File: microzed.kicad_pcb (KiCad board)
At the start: 10 copper layers, 50 x 100 mm, 334 parts, among them IC1 XC7Z020-1CLG484C, IC2 RTL8211E-VL-CG, J1 640456-3, J2 10104111-0001LF, J3 L829-1J1T-43, J4 Micro_SD_Card_Det_Hirose_DM3AT, J5 10104111-0001LF, J6 BSH-090-01-X-D-A, J7 BSH-090-01-X-D-A, Q1 MMBT3904, Q2 MMBT3904, SW1 SW_Push, U1 TLV62130RGTR, U10 MT41K256M16TW, U11 MT25QL128ABA8E12-1SIT, U12 USB3320C-EZK, U13 ASDMB-24.000MHZ-LC-T, U14 ASDMB-25.000MHZ-LC-T, U15 TXS02612RTWR, U16 CP2104-F03-GM, U2 TLV62130RGTR, U3 TLV62130RGTR, U4 TLV62130RGTR, U5 TLV62130RGTR, U6 ASDMB-33.333MHZ-LC-T, U7 TPS51206DSQR, U8 REF3012, U9 MT41K256M16TW

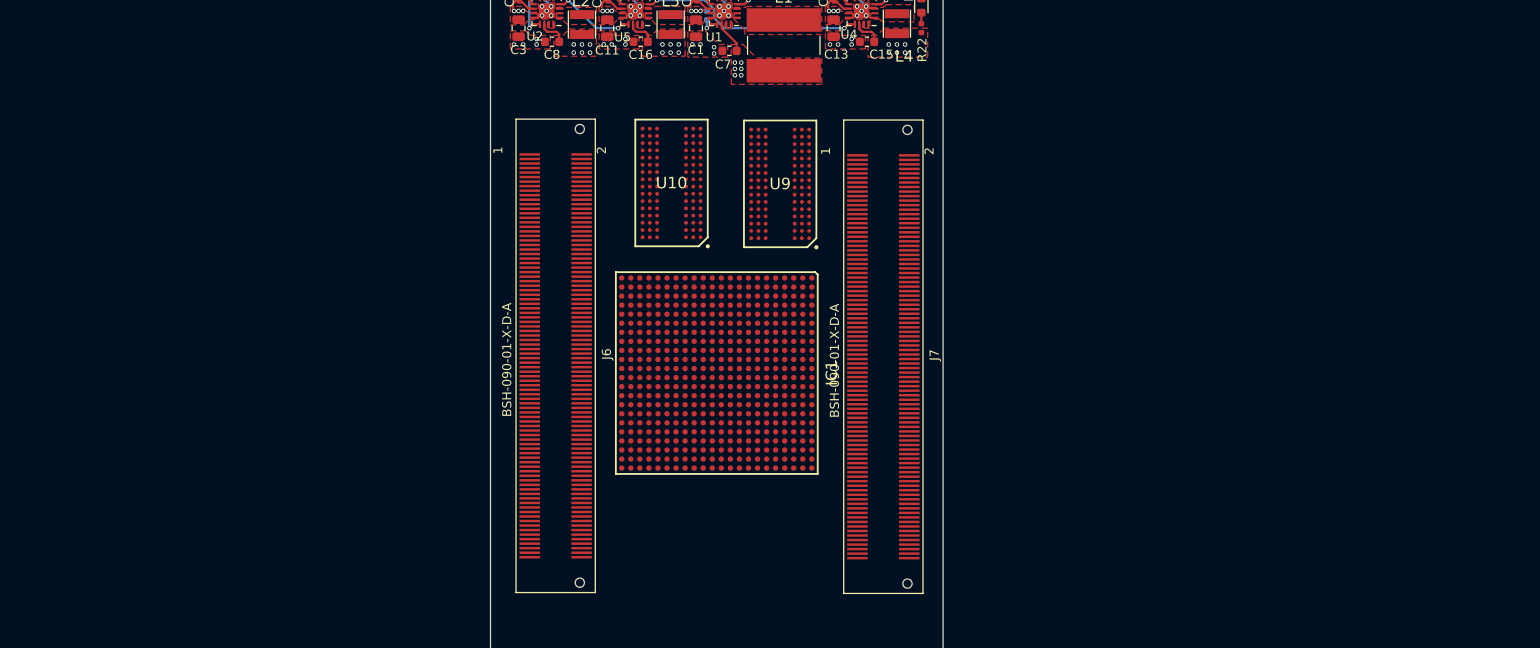
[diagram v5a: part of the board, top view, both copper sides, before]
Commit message: fix footprint & 3d model for xc7z020-clg484. (pin pitch 1.0mm -> 0.8mm)
Signed-off-by: Yi Qingliang <niqingliang2003@gmail.com>
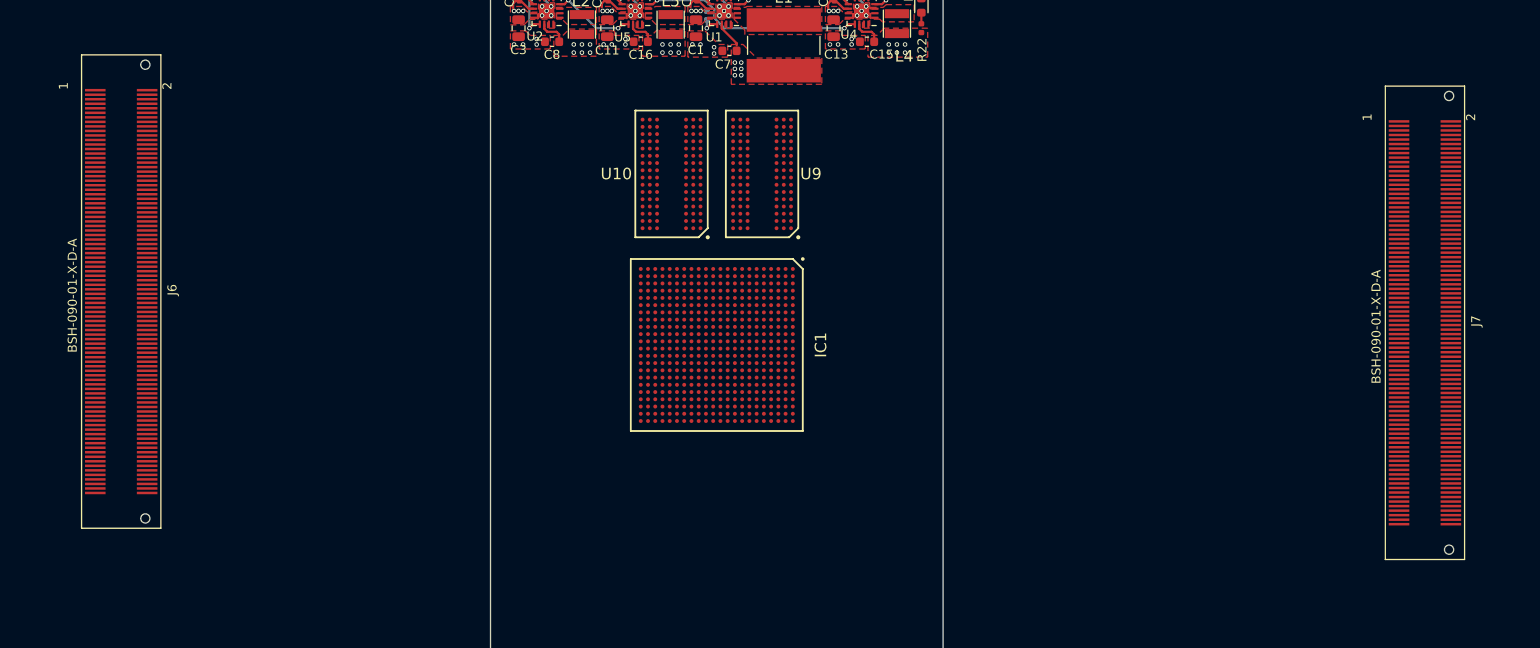
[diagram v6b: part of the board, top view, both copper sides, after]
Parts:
- IC1: footprint microzed:BGA484C100P22X22_2300X2300X254 -> microzed:BGA-484_19.0x19.0mm_Layout22x22_P0.8mm
- moved J7 60.0 mm to (78.2, 44.5)
- moved J6 48.5 mm to (-65.8, 41.0)
- moved IC1 3.10 mm to (0.00, 46.9)
- moved U9 2.28 mm to (5.00, 28.0)
- moved U10 1.00 mm to (-5.00, 28.0)

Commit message: misc update
Signed-off-by: Yi Qingliang <niqingliang2003@gmail.com>
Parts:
- J6, J7: moved to B.Cu
- moved J7 59.8 mm to (18.4, 43.7)
- moved J6 47.5 mm to (-18.4, 43.7)

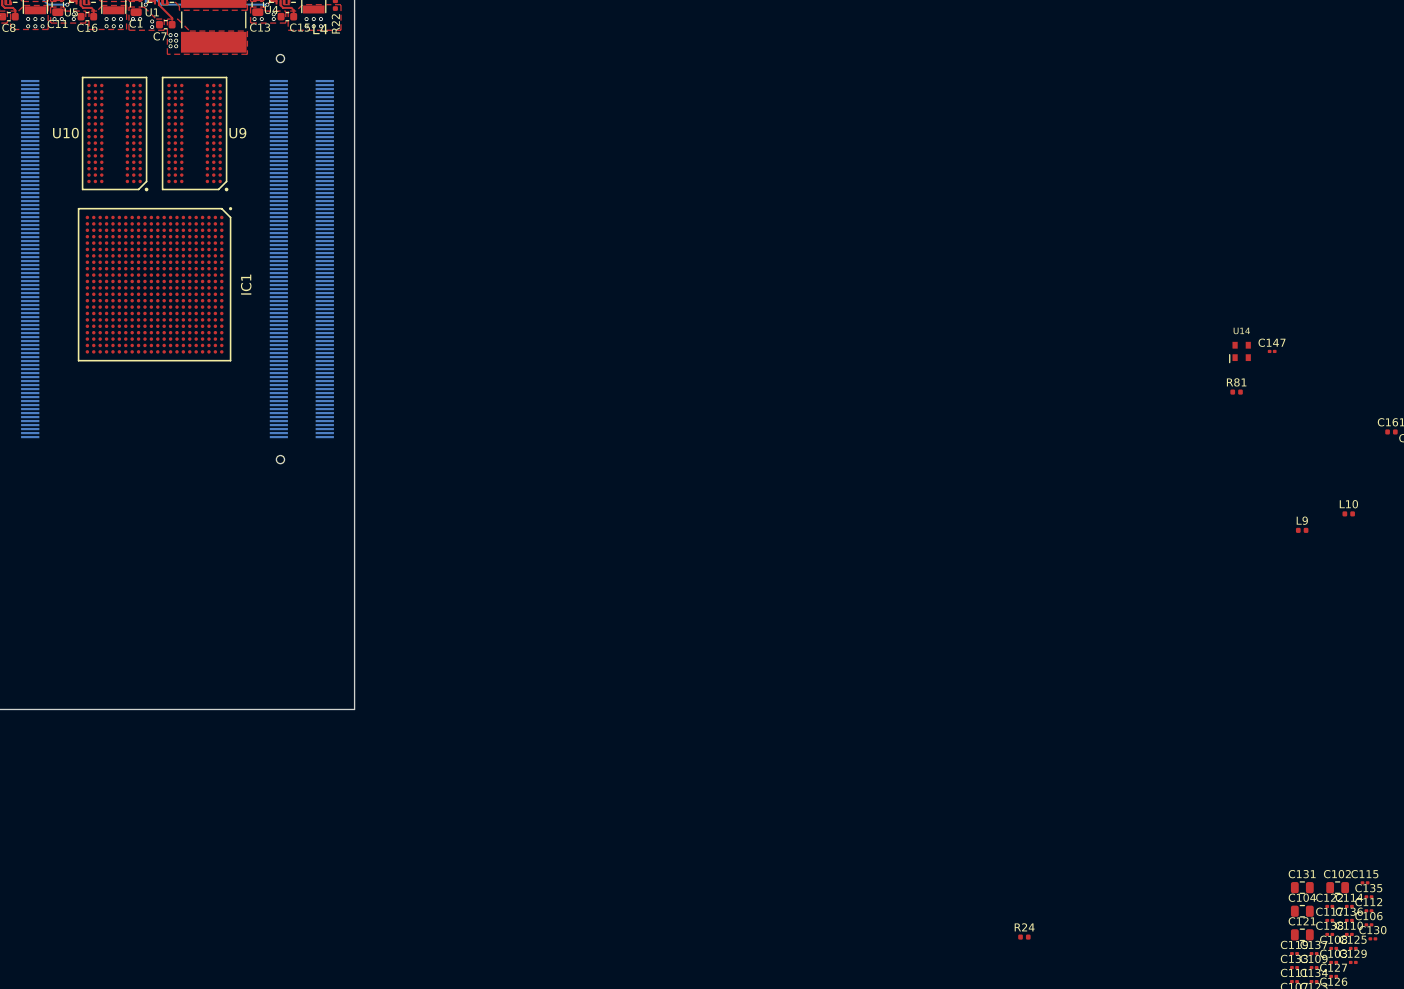
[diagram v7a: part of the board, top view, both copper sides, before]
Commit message: fix footprint for BGA-96/BGA-484
Signed-off-by: Yi Qingliang <niqingliang2003@gmail.com>
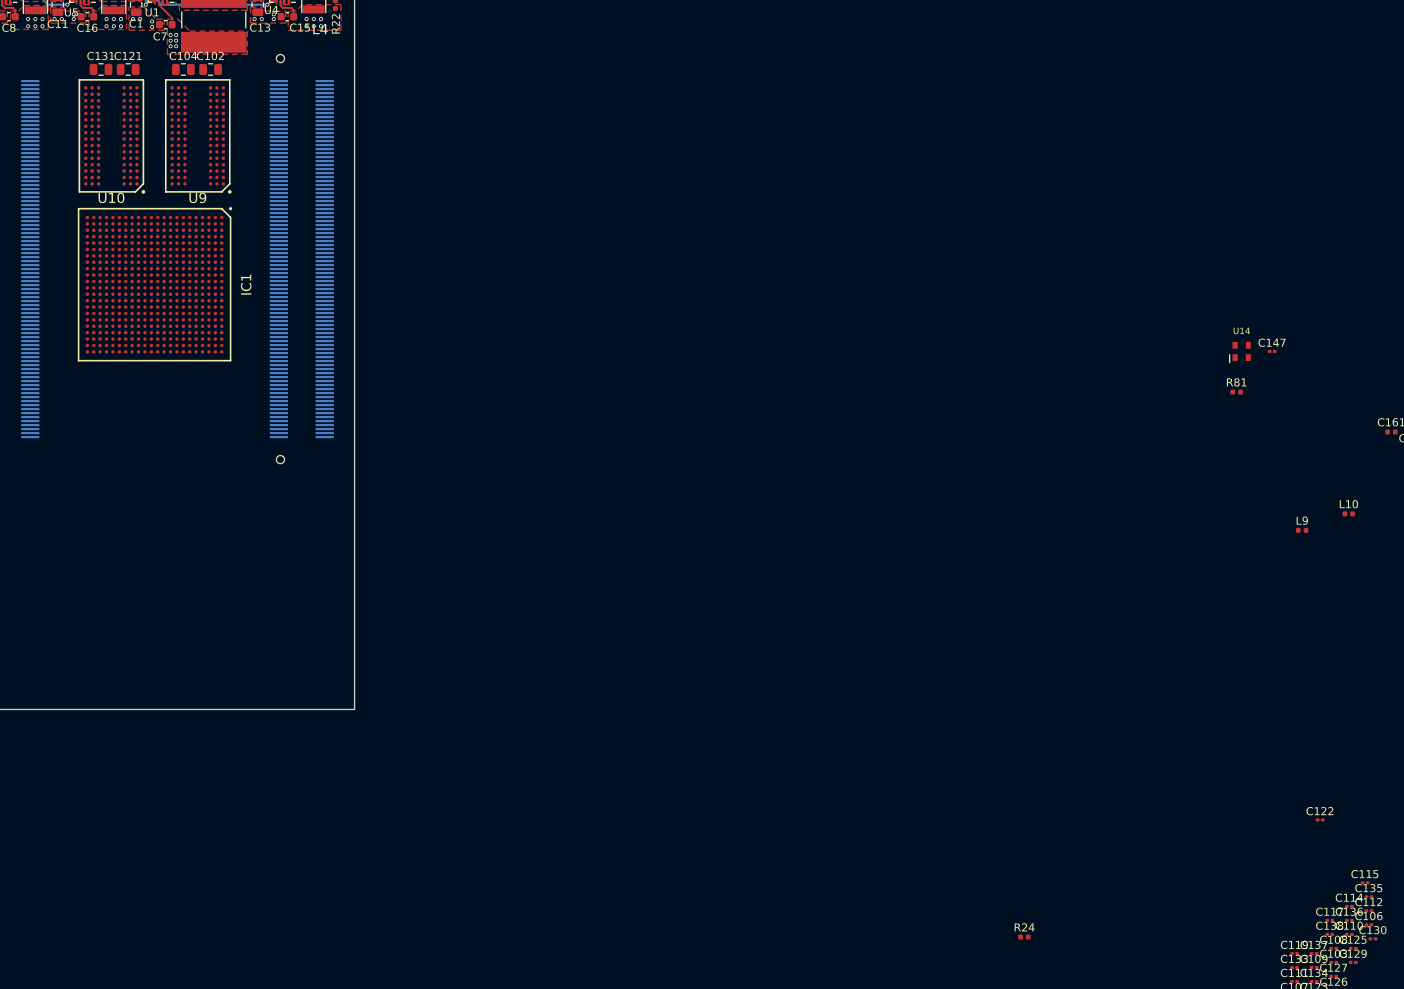
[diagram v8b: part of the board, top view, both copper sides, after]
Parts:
- U10, U9: footprint microzed:BGA96C80P9X16_800X1400X120 -> microzed:BGA-96_8.0x14.0mm_Layout2x3x16_P0.8mm
- moved C121 182.3 mm to (-3.30, 20.0)
- moved C131 181.7 mm to (-6.70, 20.0)
- moved C104 175.0 mm to (3.60, 20.0)
- moved C102 174.1 mm to (7.00, 20.0)
- moved C122 10.9 mm to (145.7, 113.8)
- moved U10 0.50 mm to (-5.40, 28.3)
- moved U9 0.50 mm to (5.40, 28.3)
